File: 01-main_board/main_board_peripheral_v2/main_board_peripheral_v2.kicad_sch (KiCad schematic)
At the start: 20 parts, among them J2 T4040014041000, J3 T4041017041-000, J4 DF12NB_5.0_-20DP-0.5V_51_, Q1 SSF2302, U1 LM74610QDGKRQ1, U2 TPS613222ADBVR, U3 NC7WZ14P6X

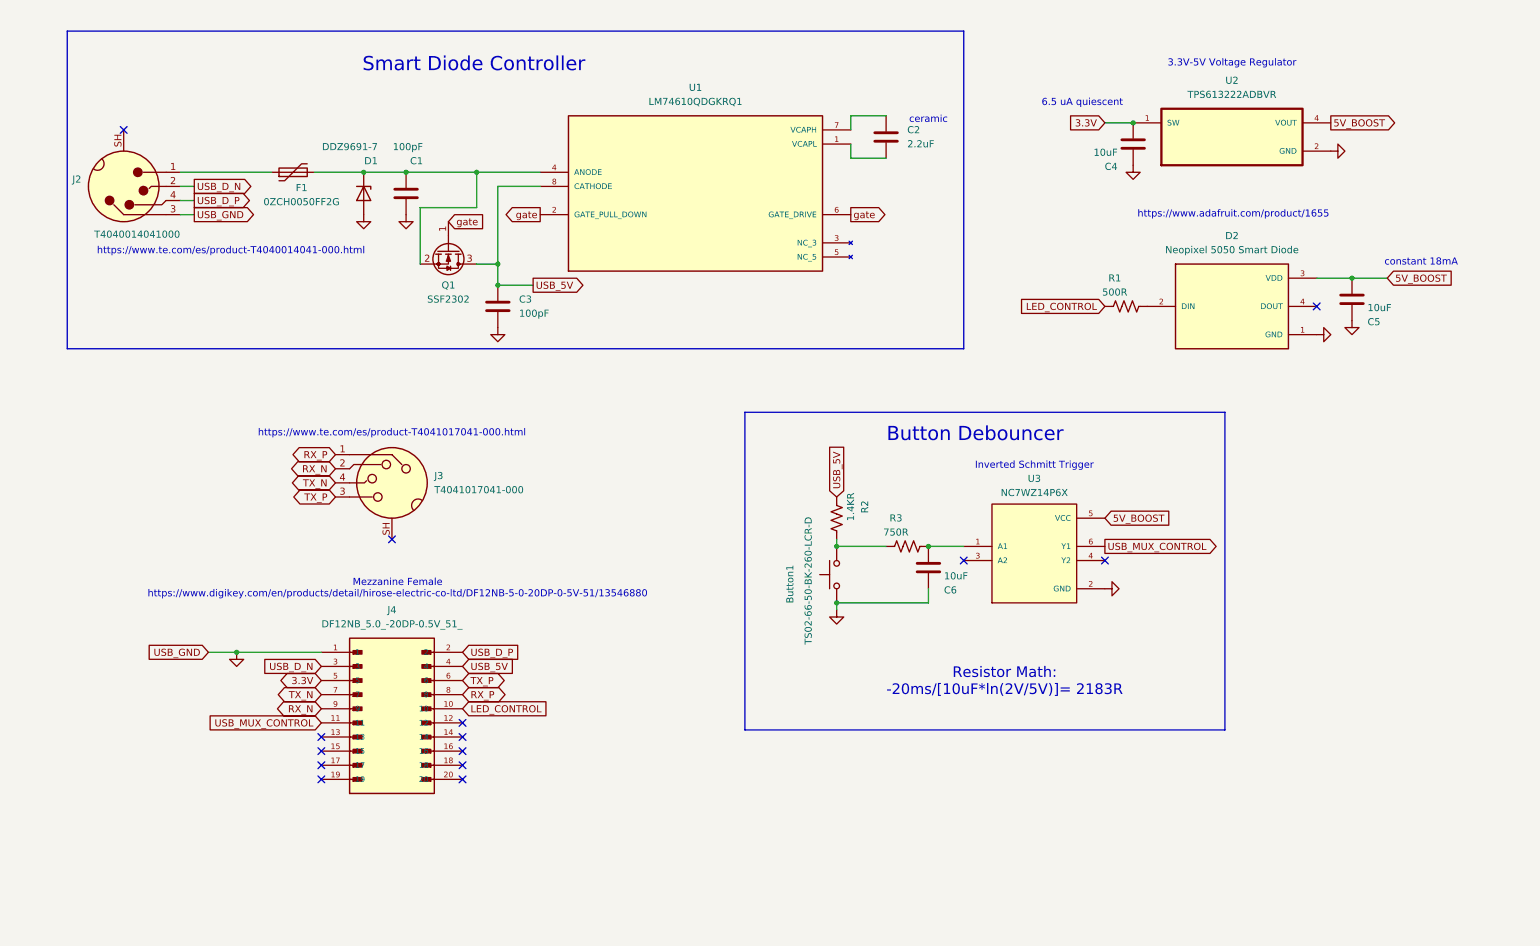
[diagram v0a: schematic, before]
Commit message: Added new buttons for schmitt trigger
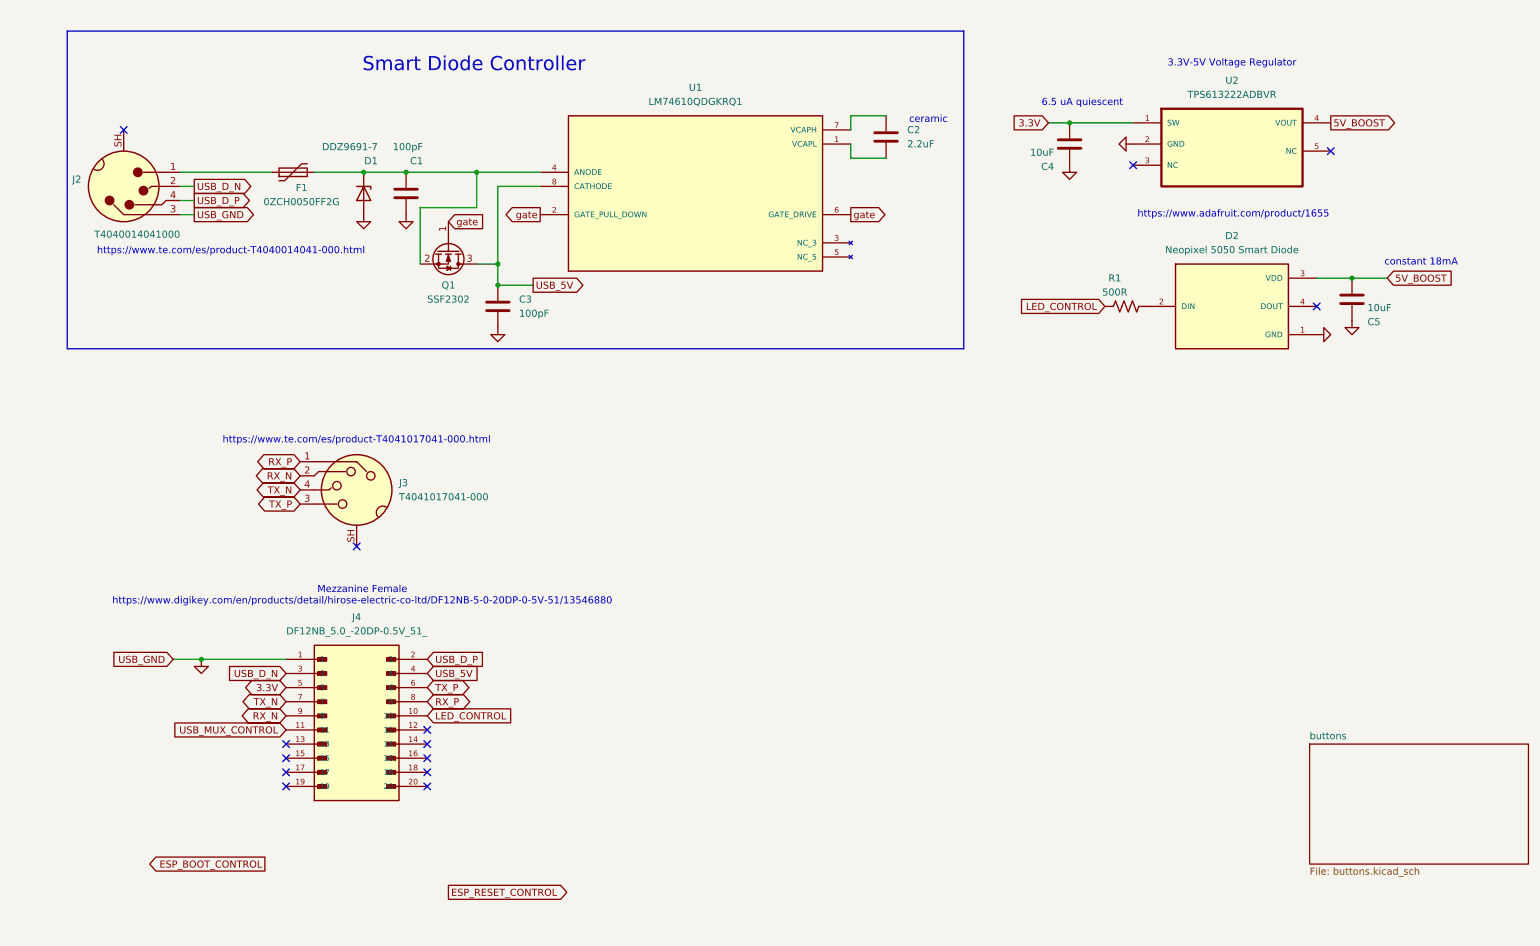
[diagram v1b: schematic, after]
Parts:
- removed Button1: TS02-66-50-BK-260-LCR-D, 22XT_Main_Peripheral:TS02-66-50-BK-260-LCR-D, symbol Switch:SW_MEC_5G
- removed C6: 10uF, 22XT_Main_Peripheral:CGA4J1X7R0J106K125AC, symbol Device:C
- removed R2: 1.4KR, 22XT_Main_Peripheral:RC1206FR-071K4L, symbol Device:R_US
- removed R3: 750R, 22XT_Main_Peripheral:RMCF1206JT750R, symbol Device:R_US
- removed U3: NC7WZ14P6X, 22XT_Main_Peripheral:NC7WZ14P6X., symbol NC7WZ14P6X:NC7WZ14P6X
- C1, C3: footprint 22XT_Main_Peripheral:CC0402JRNPO9BN101 -> Capacitor_SMD:C_0402_1005Metric
- C2: footprint 22XT_Main_Peripheral:JMK107B7225KAHTR -> Capacitor_SMD:C_0402_1005Metric
- C4, C5: footprint 22XT_Main_Peripheral:CGA4J1X7R0J106K125AC -> Capacitor_SMD:C_0603_1608Metric
- R1: footprint 22XT_Main_Peripheral:RT0603BRD07500RL -> Resistor_SMD:R_0402_1005Metric
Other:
- added sheet buttons (buttons.kicad_sch)
- note removed: "Button Debouncer"
- note removed: "Inverted Schmitt Trigger"
- note removed: "Resistor Math: -20ms/[10uF*ln(2V/5V)]= 2183R"
- moved on the sheet: C4, J3, J4

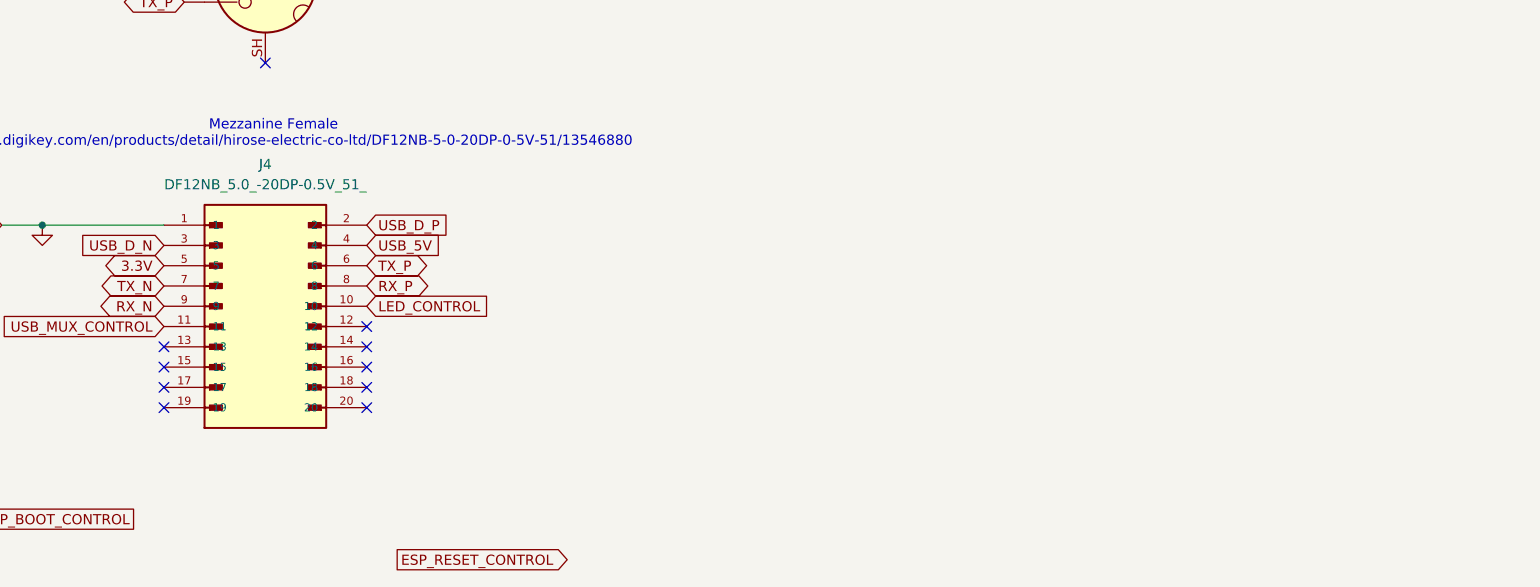
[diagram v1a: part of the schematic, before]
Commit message: Finished silkscreen
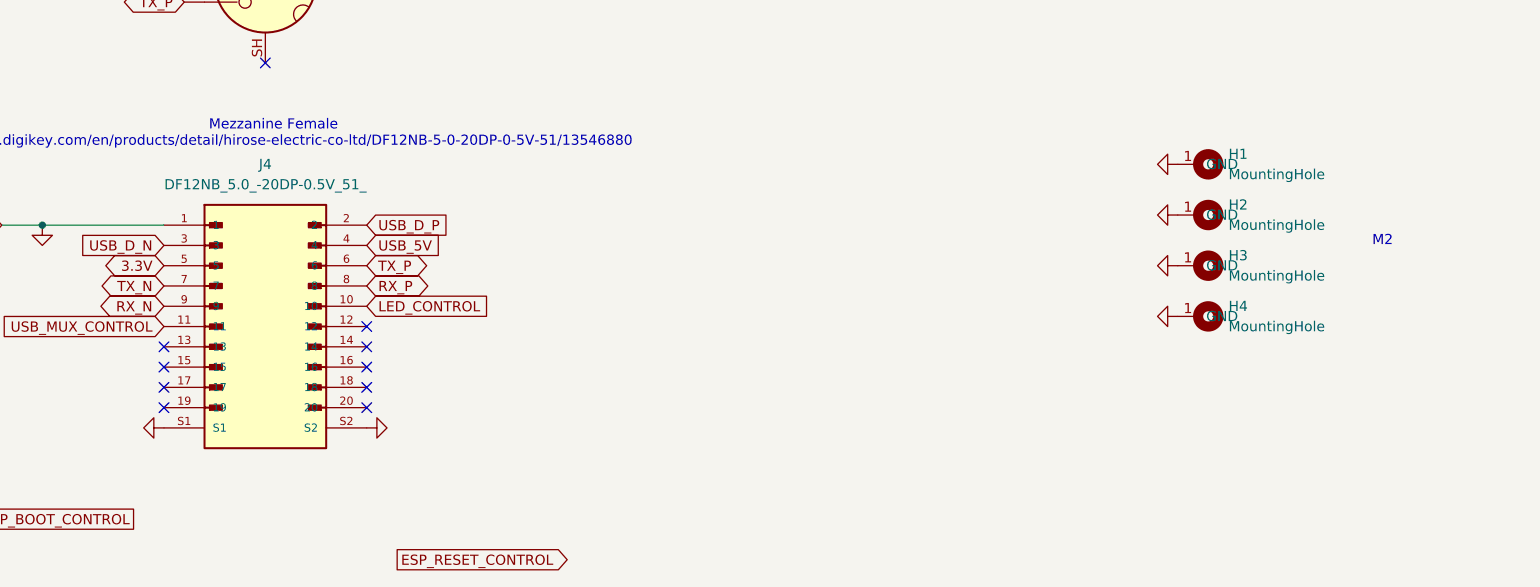
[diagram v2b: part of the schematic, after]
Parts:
- added H1, H2, H3, H4: MountingHole, MountingHole:MountingHole_2.2mm_M2_Pad, symbol Mechanical:MountingHole
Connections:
- net GND: now also J4.S1, J4.S2, H1.1 (GND), H2.1 (GND), H3.1 (GND), H4.1 (GND)
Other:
- note added: "M2"

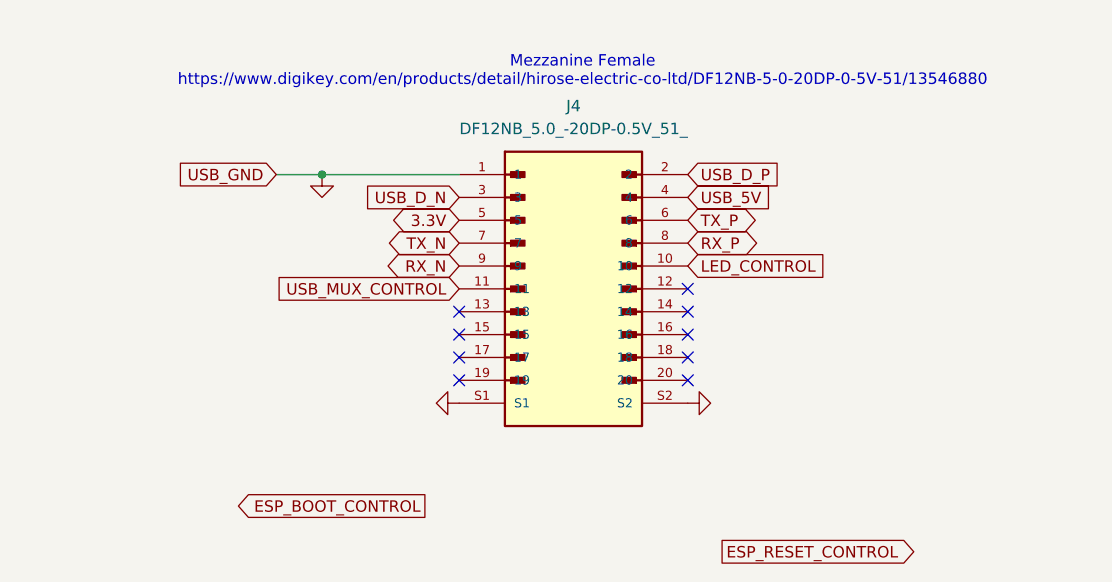
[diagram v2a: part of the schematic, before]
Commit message: fixed schematic and connected layout
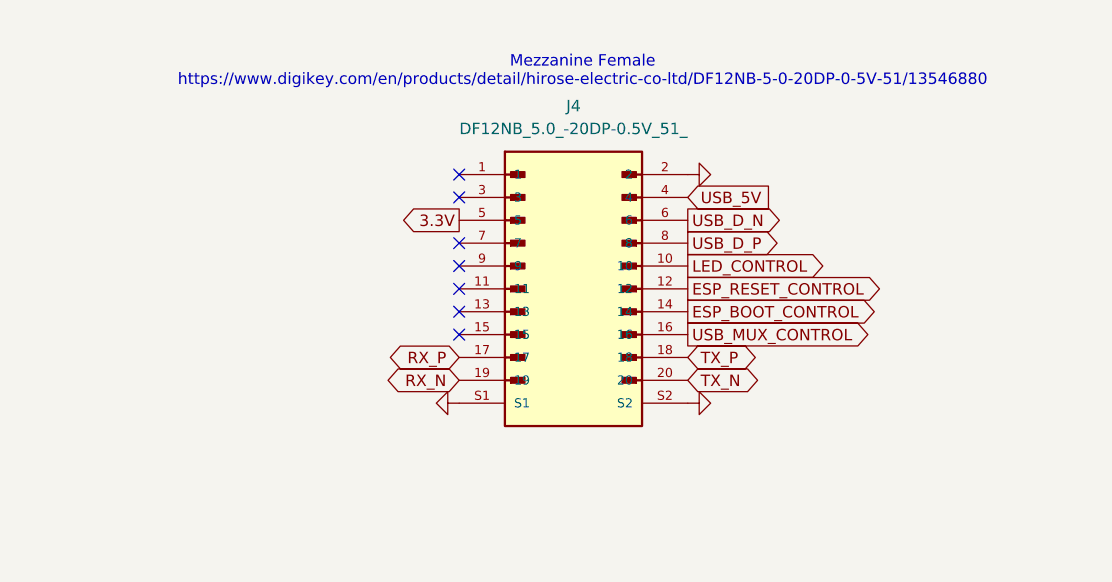
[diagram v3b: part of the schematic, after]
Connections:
- net ESP_BOOT_CONTROL: now also J4.14
- net ESP_RESET_CONTROL: now also J4.12
- net GND: now also J4.2; no longer J2.3, J4.1
- net RX_N: now also J4.19; no longer J4.9
- net RX_P: now also J4.17; no longer J4.8
- net TX_N: now also J4.20; no longer J4.7
- net TX_P: now also J4.18; no longer J4.6
- net USB_D_N: now also J4.6; no longer J4.3
- net USB_D_P: now also J4.8; no longer J4.2
- net USB_MUX_CONTROL: now also J4.16; no longer J4.11
- new net USB_GND: J2.3
- no-connect marks 14 -> 12

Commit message: finished layout
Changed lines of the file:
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@@
 	)
 	(global_label "USB_5V"
-		(shape input)
+		(shape output)
 		(at 83.82 134.62 0)
 		(fields_autoplaced yes)

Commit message: layout done
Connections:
- net USB_GND is gone; now on net GND: J2.3
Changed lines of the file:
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@@
 	(wire
 		(pts
-			(xy 39.37 52.07) (xy 41.91 52.07)
+			(xy 82.55 50.8) (xy 82.55 60.96)
 		)
 		(stroke
@@
 		)
 	)
-	(wire
+	(bus
 		(pts
-			(xy 82.55 50.8) (xy 82.55 60.96)
+			(xy 180.34 19.05) (xy 19.05 19.05)
 		)
 		(stroke
@@
 	(bus
 		(pts
-			(xy 180.34 19.05) (xy 19.05 19.05)
+			(xy 180.34 19.05) (xy 180.34 76.2)
 		)
 		(stroke
@@
 		)
 	)
-	(bus
+	(wire
 		(pts
-			(xy 180.34 19.05) (xy 180.34 76.2)
+			(xy 160.02 34.29) (xy 166.37 34.29)
 		)
 		(stroke
@@
 	(wire
 		(pts
-			(xy 160.02 34.29) (xy 166.37 34.29)
+			(xy 104.14 46.99) (xy 96.52 46.99)
 		)
 		(stroke
@@
 		)
 	)
-	(wire
+	(bus
 		(pts
-			(xy 104.14 46.99) (xy 96.52 46.99)
+			(xy 19.05 76.2) (xy 180.34 76.2)
 		)
 		(stroke
@@
 		)
 	)
-	(bus
+	(wire
 		(pts
-			(xy 19.05 76.2) (xy 180.34 76.2)
+			(xy 96.52 60.96) (xy 92.71 60.96)
 		)
 		(stroke
@@
 		)
 	)
-	(wire
+	(bus
 		(pts
-			(xy 96.52 60.96) (xy 92.71 60.96)
+			(xy 19.05 19.05) (xy 19.05 76.2)
 		)
 		(stroke
@@
 		)
 	)
-	(bus
+	(wire
 		(pts
-			(xy 19.05 19.05) (xy 19.05 76.2)
+			(xy 96.52 64.77) (xy 102.87 64.77)
 		)
 		(stroke
@@
 	(wire
 		(pts
-			(xy 96.52 64.77) (xy 102.87 64.77)
+			(xy 63.5 44.45) (xy 72.39 44.45)
 		)
 		(stroke
@@
 	(wire
 		(pts
-			(xy 63.5 44.45) (xy 72.39 44.45)
+			(xy 256.54 63.5) (xy 250.19 63.5)
 		)
 		(stroke
@@
 	(wire
 		(pts
-			(xy 256.54 63.5) (xy 250.19 63.5)
+			(xy 160.02 36.83) (xy 160.02 34.29)
 		)
 		(stroke
@@
 		)
 	)
-	(wire
-		(pts
-			(xy 160.02 36.83) (xy 160.02 34.29)
-		)
-		(stroke
-			(width 0)
-			(type default)
-		)
-	)
 	(global_label "RX_P"
 		(shape bidirectional)
@@
 		(property "Intersheetrefs" "${INTERSHEET_REFS}"
 			(at 97.0425 52.07 0)
-			(effects
-				(font
-					(size 1.27 1.27)
-				)
-				(justify right)
-				(hide yes)
-			)
-		)
-	)
-	(global_label "USB_GND"
-		(shape output)
-		(at 41.91 52.07 0)
-		(fields_autoplaced yes)
-		(effects
-			(font
-				(size 1.27 1.27)
-			)
-			(justify left)
-		)
-		(property "Intersheetrefs" "${INTERSHEET_REFS}"
-			(at 30.2767 52.07 0)
 			(effects
 				(font
@@
 					(unit 1)
 				)
+			)
+		)
+	)
+	(symbol
+		(lib_id "power:GND")
+		(at 39.37 52.07 90)
+		(unit 1)
+		(exclude_from_sim no)
+		(in_bom yes)
+		(on_board yes)
+		(dnp no)
+		(fields_autoplaced yes)
+		(property "Reference" "#PWR01"
+			(at 45.72 52.07 0)
+			(effects
+				(font
+					(size 1.27 1.27)
+				)
+				(hide yes)
+			)
+		)
+		(property "Value" "GND"
+			(at 44.45 52.07 0)
+			(effects
+				(font
+					(size 1.27 1.27)
+				)
+				(hide yes)
+			)
+		)
+		(property "Footprint" ""
+			(at 39.37 52.07 0)
+			(effects
+				(font
+					(size 1.27 1.27)
+				)
+				(hide yes)
+			)
+		)
+		(property "Datasheet" ""
+			(at 39.37 52.07 0)
+			(effects
+				(font
+					(size 1.27 1.27)
+				)
+				(hide yes)
+			)
+		)
+		(property "Description" "Power symbol creates a global label with name \"GND\" , ground"
+			(at 39.37 52.07 0)
+			(effects
+				(font
+					(size 1.27 1.27)
+				)
+				(hide yes)
+			)
+		)
+		(pin "1"
+		)
+		(instances
+			(project "main_board_peripheral_v2"
+				(path "/3f673207-cdae-494a-ab60-6e58b06fb202"
+					(reference "#PWR01")
+					(unit 1)
+				)

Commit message: Push to change computers. New schematic.
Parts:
- removed J4: DF12NB_5.0_-20DP-0.5V_51_, 22XT_Main_Peripheral:DF12NB_5.0_-20DP-0.5V_51_, symbol DF12NB_5.0_-20DP-0.5V_51_:DF12NB_5.0_-20DP-0.5V_51_
- removed U2: TPS613222ADBVR, 22XT_Main_Peripheral:TPS613222ADBVR, symbol TPS613222ADBVR:TPS613222ADBVR
- added C6: 10uF, Capacitor_SMD:C_0603_1608Metric, symbol Device:C
- added J1: 1-84952-0, CONN10_1-84982-0_TEC, symbol 2026-02-06_01-22-38:1-84982-0
- added PS1: TPSM83100SIUR, TPSM83100SIUR, symbol 2026-02-06_01-22-38:TPSM83100SIUR
- added R2: 820K R, symbol Device:R_US
- added R3: 100K R, symbol Device:R_US
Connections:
- net 3.3V: now also J1.6, PS1.1 (VIN), PS1.8 (EN)
- net 5V_BOOST: now also C6.1, PS1.4 (VOUT), R2.2
- net GND: now also C6.2, J1.3, PS1.2 (GND_1), PS1.7 (MODE), R3.1
- net LED_CONTROL: now also J1.5
- net RX_N: now also J1.8
- net RX_P: now also J1.10
- net TX_N: now also J1.9
- net TX_P: now also J1.7
- net USB_5V: now also J1.4
- net USB_D_N: now also J1.1
- net USB_D_P: now also J1.2
- new net: PS1.5 (FB), R2.1, R3.2
- no-connect marks 12 -> 5
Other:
- removed sheet buttons
- note added: "FPC Connector to Main Board https://www.digikey.com/en/products/detail/te-connectivity-amp-connectors/1-84982-0/1893491"
- note removed: "Mezzanine Female https://www.digikey.com/en/products/detail/hirose-electric-co-ltd/DF12NB-5-0-20DP-0-5V-51/13546880"
- moved on the sheet: C4

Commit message: Started on layout
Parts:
- removed H1, H2, H3, H4: MountingHole, MountingHole:MountingHole_2.2mm_M2_Pad, symbol Mechanical:MountingHole
- removed J1: 1-84952-0, CONN10_1-84982-0_TEC, symbol 2026-02-06_01-22-38:1-84982-0
- added J4: FH41-15S-0.5SH_05_, 22XT_Main_Peripheral:FH4115S05SH05, symbol FH41-15S-0_5SH_05_:FH41-15S-0.5SH_05_
- added R4, R5: 30K R, 22XT_Main_Peripheral:RESC3116X65N (30K), symbol Device:R_US
- PS1: footprint TPSM83100SIUR -> 22XT_Main_Peripheral:TPSM83100SIUR
- R2: footprint (none) -> 22XT_Main_Peripheral:RESC3116X65N (820K)
- R3: value 100K R -> 30K R; footprint (none) -> 22XT_Main_Peripheral:RESC3116X65N (30K)
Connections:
- net 3.3V: now also J4.8
- net GND: now also J4.12, J4.13, J4.3, J4.4, J4.7, J4.9, J4.G1, J4.G2, J4.MP1, J4.MP2, R5.1; no longer R3.1
- net LED_CONTROL: now also J4.5
- net RX_N: now also J4.10
- net RX_P: now also J4.11
- net TX_N: now also J4.15
- net TX_P: now also J4.14
- net USB_5V: now also J4.6
- net USB_D_N: now also J4.1
- net USB_D_P: now also J4.2
- new net: R4.1, R5.2
- new net: R3.1, R4.2
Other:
- note added: "FPC Connector to Main Board https://www.digikey.com/en/products/detail/hirose-electric-co-ltd/FH41-15S-0-5SH-05/5132554"
- note added: "Resistor math: (820K R/90K R + 1)0.5 = 5.06 V"
- note removed: "FPC Connector to Main Board https://www.digikey.com/en/products/detail/te-connectivity-amp-connectors/1-84982-0/1893491"
- note removed: "M2"
- moved on the sheet: C5, D2, R1
